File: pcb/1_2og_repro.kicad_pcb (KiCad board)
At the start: 2 copper layers, 347.1 x 119.3 mm, 225 parts, among them J1 Pico EzMate, J2 548190519, J3 RAW, J4 S3B, Q1 2N7002, SW1 MX_SW_solder, SW10 MX_SW_solder, SW11 MX_SW_solder, SW12 MX_SW_solder, SW13 MX_SW_solder, SW14 MX_SW_solder, SW15 MX_SW_solder, SW16 MX_SW_solder, SW17 MX_SW_solder, SW18 MX_SW_solder, SW19 MX_SW_solder, SW2 MX_SW_solder, SW20 MX_SW_solder, SW21 MX_SW_solder, SW22 MX_SW_solder, SW23 MX_SW_solder, SW24 MX_SW_solder, SW25 MX_SW_solder, SW26 MX_SW_solder, SW27 MX_SW_solder, SW28 MX_SW_solder, SW29 MX_SW_solder, SW3 MX_SW_solder, SW30 MX_SW_solder, SW31 MX_SW_solder, SW32 MX_SW_solder, SW33 MX_SW_solder, SW34 MX_SW_solder, SW35 MX_SW_solder, SW36 MX_SW_solder, SW37 MX_SW_solder, SW38 MX_SW_solder, SW39 MX_SW_solder, SW4 MX_SW_solder, SW40 MX_SW_solder, SW41 MX_SW_solder, SW42 MX_SW_solder, SW43 MX_SW_solder, SW44 MX_SW_solder, SW45 MX_SW_solder, SW46 MX_SW_solder, SW47 MX_SW_solder, SW48 MX_SW_solder, SW49 MX_SW_solder, SW5 MX_SW_solder, SW50 MX_SW_solder, SW51 MX_SW_solder, SW52 MX_SW_solder, SW53 MX_SW_solder, SW54 MX_SW_solder, SW55 MX_SW_solder, SW56 MX_SW_solder, SW57 MX_SW_solder, SW58 MX_SW_solder, SW59 MX_SW_solder, SW6 MX_SW_solder, SW60 MX_SW_solder, SW61 MX_SW_solder, SW62 MX_SW_solder, SW63 MX_SW_solder, SW64 MX_SW_solder, SW65 MX_SW_solder, SW66 MX_SW_solder, SW67 MX_SW_solder, SW68 MX_SW_solder, SW69 MX_SW_solder, SW7 MX_SW_solder, SW70 MX_SW_solder, SW71 MX_SW_solder, SW72 MX_SW_solder, SW73 MX_SW_solder, SW74 MX_SW_solder, SW75 MX_SW_solder, SW76 MX_SW_solder, SW77 MX_SW_solder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

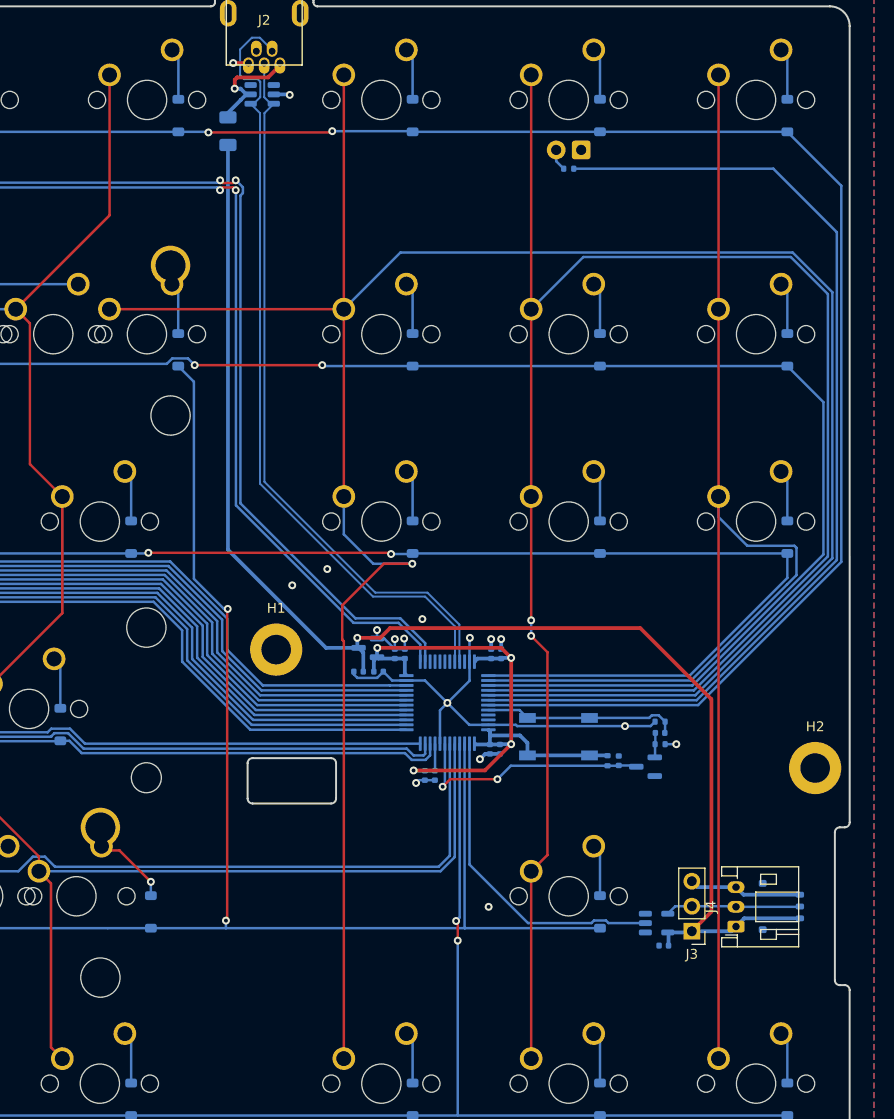
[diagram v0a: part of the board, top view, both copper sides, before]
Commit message: update gerbers, change mounting hole dimensions
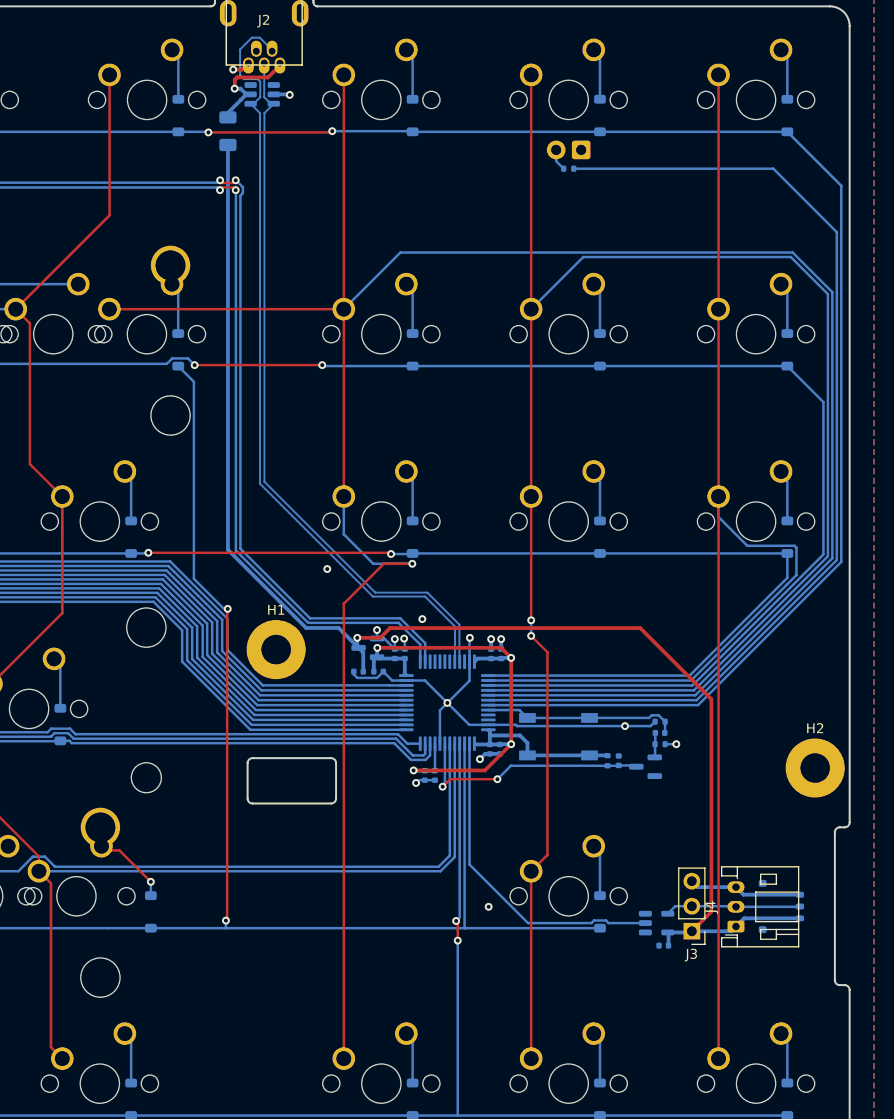
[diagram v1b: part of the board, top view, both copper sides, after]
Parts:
- H1, H2: footprint MountingHole:MountingHole_3.2mm_M3_Pad -> MountingHole:MountingHole_3mm_Pad
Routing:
- net NUMLOCKLED: track 335.0 -> 337.7 mm
- net CAPS_LED: track 404.1 -> 406.8 mm
- net GND: track 76.1 -> 76.3 mm, vias 18 -> 17

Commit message: ok juggle a few pins around
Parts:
- moved SW95 7.09 mm to (336.7, 87.3)
- moved R1 5.21 mm to (339.3, 90.9), turned to 180 degrees
- moved C12 4.73 mm to (344.6, 86.9)
- moved R5 4.73 mm to (344.6, 85.8)
- moved Q1 4.73 mm to (343.1, 90.4)
- moved R6 4.73 mm to (344.6, 88.1)
- moved R3 3.02 mm to (332.9, 30.6)
- moved C11 2.72 mm to (337.3, 90.9), turned to 180 degrees
- moved D30 2.48 mm to (263.5, 48.0)
- moved D47 2.48 mm to (288.5, 67.1)
- moved D86 2.48 mm to (288.5, 124.1)
- moved SW31 2.48 mm to (271.1, 46.5)
- moved SW92 2.48 mm to (313.9, 122.5)
- moved SW14 2.48 mm to (313.9, 22.7)
- moved SW32 2.48 mm to (313.9, 46.5)
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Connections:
- U2 pad 2: RGBLED -> unconnected-(U2-PC13-Pad2)
- U2 pad 27: unconnected-(U2-PB14-Pad27) -> ROW2
- U2 pad 28: unconnected-(U2-PB15-Pad28) -> ROW5
- U2 pad 3: ROW4 -> unconnected-(U2-PC14-Pad3)
- U2 pad 37: ROW2 -> unconnected-(U2-PA14-Pad37)
- U2 pad 4: ROW5 -> unconnected-(U2-PC15-Pad4)
- U2 pad 45: unconnected-(U2-PB8-Pad45) -> RGBLED
- U2 pad 46: unconnected-(U2-PB9-Pad46) -> ROW4
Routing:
- net ROW5: track 361.3 -> 405.5 mm
- net ROW2: track 360.4 -> 347.3 mm, vias 2 -> 3
- net RGBLED: track 32.8 -> 45.1 mm, vias 0 -> 2
- net ROW4: track 375.4 -> 385.1 mm, vias 2 -> 4
- net GND: track 76.3 -> 68.2 mm, vias 17 -> 16
- net COL14: track 254.8 -> 247.2 mm
- net +3V3: track 68.6 -> 72.6 mm
- net NRST: track 25.1 -> 28.4 mm
- net BOOT0: track 19.8 -> 22.2 mm
- net Net-(D91-A): track 2.22 -> 3.17 mm
- net COL15: track 201.8 -> 202.6 mm

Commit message: tune differential pair, reroute to remove redundant vias
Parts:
- moved U3 2.27 mm to (301.8, 24.4)
- moved F1 0.95 mm to (298.3, 26.8)
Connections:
- U3 pad 1: unconnected-(U3-IO1-Pad1) -> D+
- U3 pad 3: D+ -> unconnected-(U3-IO2-Pad3)
- U3 pad 4: D- -> unconnected-(U3-IO3-Pad4)
- U3 pad 6: unconnected-(U3-IO4-Pad6) -> D-
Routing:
- net VBUS: track 11.3 -> 18.6 mm, vias 1 -> 0
- net CAPS_LED: track 406.8 -> 413.9 mm, vias 2 -> 0
- net NUMLOCKLED: track 337.5 -> 343.5 mm, vias 2 -> 0
- net D+: track 73.3 -> 79.0 mm
- net GND: track 68.2 -> 69.9 mm, vias 16 -> 17
- net D-: track 80.7 -> 79.1 mm
- net ROW4: track 385.1 -> 384.1 mm
- net RGBLED: track 45.1 -> 44.1 mm
- net +5V: track 141.2 -> 140.3 mm
